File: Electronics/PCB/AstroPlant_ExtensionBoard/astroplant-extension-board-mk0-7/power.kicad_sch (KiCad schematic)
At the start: 13 parts, among them J14 61300621121, J20 691102710002, J21 691102710002

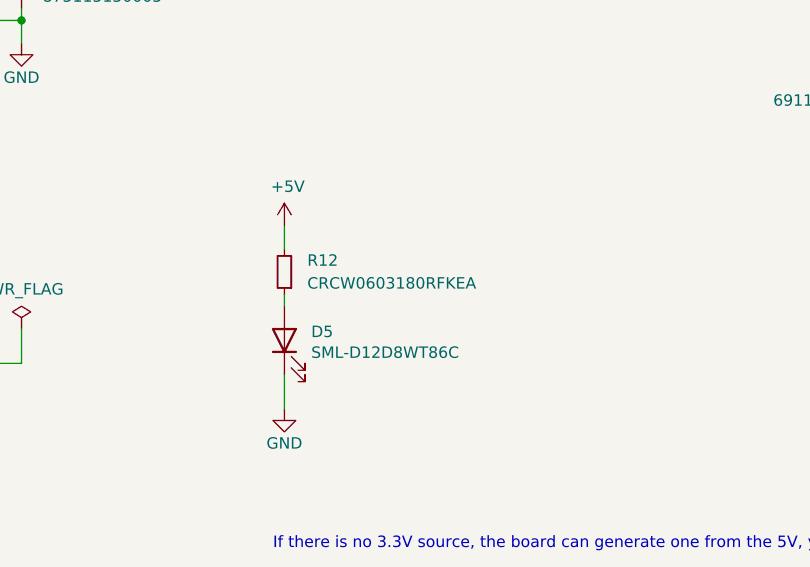
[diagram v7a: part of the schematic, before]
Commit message: Fix the antenna (Implies a change in PCB routing)+ improve readme (add a tutorial to make the board on eurocicruit).
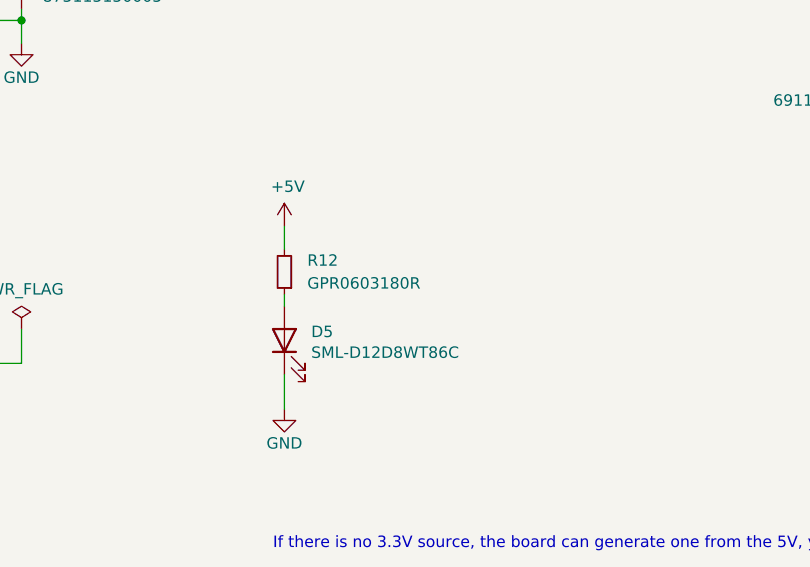
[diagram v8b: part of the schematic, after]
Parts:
- C15: footprint CAPC1608X50N -> Capacitor_SMD:C_0603_1608Metric; Arrow Price/Stock https://www.arrow.com/en/products/grm185r61c105ke44d/murata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 -> (none); Height 0.5 -> (none); MPN GRM185R61C105KE44D -> GPC0603105-16; Manufacturer_Name Murata Electronics -> (none); Manufacturer_Part_Number GRM185R61C105KE44D -> (none); Mouser Part Number 81-GRM185R61C105KE44 -> (none); Mouser Price/Stock https://www.mouser.co.uk/ProductDetail/Murata-Electronics/G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 -> (none)
- C16: footprint CAPC1608X50N -> Capacitor_SMD:C_0603_1608Metric; Arrow Price/Stock https://www.arrow.com/en/products/grm185r61c105ke44d/murata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 -> (none); Height 0.5 -> (none); MPN GRM185R61C105KE44D -> GPC0603105-16; Manufacturer_Name Murata Electronics -> (none); Manufacturer_Part_Number GRM185R61C105KE44D -> GPC0603105-16; Mouser Part Number 81-GRM185R61C105KE44 -> (none); Mouser Price/Stock https://www.mouser.co.uk/ProductDetail/Murata-Electronics/G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 -> (none)
- R12: value CRCW0603180RFKEA -> GPR0603180R; MPN CRCW0603180RFKEA -> GPR0603180R
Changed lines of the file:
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@@
       (effects (font (size 1.27 1.27)) (justify left))
     )
-    (property "Footprint" "CAPC1608X50N" (at 231.14 153.67 0)
-      (effects (font (size 1.27 1.27)) (justify left) hide)
-    )
-    (property "Datasheet" "https://componentsearchengine.com/Datasheets/2/GRM185R61C105KE44D.pdf" (at 228.6 153.67 0)
-      (effects (font (size 1.27 1.27)) (justify left) hide)
-    )
-    (property "Description" "MURATA - GRM185R61C105KE44D - CAP, MLCC, X5R, 1UF, 16V, 0603" (at 226.06 153.67 0)
-      (effects (font (size 1.27 1.27)) (justify left) hide)
-    )
-    (property "Height" "0.5" (at 223.52 153.67 0)
-      (effects (font (size 1.27 1.27)) (justify left) hide)
-    )
-    (property "Manufacturer_Name" "Murata Electronics" (at 220.98 153.67 0)
-      (effects (font (size 1.27 1.27)) (justify left) hide)
-    )
-    (property "Manufacturer_Part_Number" "GRM185R61C105KE44D" (at 218.44 153.67 0)
-      (effects (font (size 1.27 1.27)) (justify left) hide)
-    )
-    (property "Mouser Part Number" "81-GRM185R61C105KE44" (at 215.9 153.67 0)
-      (effects (font (size 1.27 1.27)) (justify left) hide)
-    )
-    (property "Mouser Price/Stock" "https://www.mouser.co.uk/ProductDetail/Murata-Electronics/GRM185R61C105KE44D?qs=c4yvaafl%252BAw5enNBKMnY3A%3D%3D" (at 213.36 153.67 0)
-      (effects (font (size 1.27 1.27)) (justify left) hide)
-    )
-    (property "MPN" "GRM185R61C105KE44D" (at 210.82 153.67 0)
-      (effects (font (size 1.27 1.27)) (justify left) hide)
-    )
-    (property "Arrow Price/Stock" "https://www.arrow.com/en/products/grm185r61c105ke44d/murata-manufacturing" (at 208.28 153.67 0)
+    (property "Footprint" "Capacitor_SMD:C_0603_1608Metric" (at 231.14 153.67 0)
+      (effects (font (size 1.27 1.27)) (justify left) hide)
+    )
+    (property "Datasheet" "" (at 228.6 153.67 0)
+      (effects (font (size 1.27 1.27)) (justify left) hide)
+    )
+    (property "Manufacturer_Part_Number" "GPC0603105-16" (at 218.44 153.67 0)
+      (effects (font (size 1.27 1.27)) (justify left) hide)
+    )
+    (property "MPN" "GPC0603105-16" (at 210.82 153.67 0)
       (effects (font (size 1.27 1.27)) (justify left) hide)
     )
@@
       (effects (font (size 1.27 1.27)) (justify right))
     )
-    (property "Value" "CRCW0603180RFKEA" (at 120.65 99.06 0)
+    (property "Value" "GPR0603180R" (at 120.65 99.06 0)
       (effects (font (size 1.27 1.27)) (justify right))
     )
@@
       (effects (font (size 1.27 1.27)) hide)
     )
-    (property "MPN" "CRCW0603180RFKEA" (at 118.11 97.79 0)
+    (property "MPN" "GPR0603180R" (at 118.11 97.79 0)
       (effects (font (size 1.27 1.27)) hide)
     )
@@
       (effects (font (size 1.27 1.27)) (justify left))
     )
-    (property "Footprint" "CAPC1608X50N" (at 181.61 148.59 0)
-      (effects (font (size 1.27 1.27)) (justify left) hide)
-    )
-    (property "Datasheet" "https://componentsearchengine.com/Datasheets/2/GRM185R61C105KE44D.pdf" (at 179.07 148.59 0)
-      (effects (font (size 1.27 1.27)) (justify left) hide)
-    )
-    (property "Description" "MURATA - GRM185R61C105KE44D - CAP, MLCC, X5R, 1UF, 16V, 0603" (at 176.53 148.59 0)
-      (effects (font (size 1.27 1.27)) (justify left) hide)
-    )
-    (property "Height" "0.5" (at 173.99 148.59 0)
-      (effects (font (size 1.27 1.27)) (justify left) hide)
-    )
-    (property "Manufacturer_Name" "Murata Electronics" (at 171.45 148.59 0)
-      (effects (font (size 1.27 1.27)) (justify left) hide)
-    )
-    (property "Manufacturer_Part_Number" "GRM185R61C105KE44D" (at 168.91 148.59 0)
-      (effects (font (size 1.27 1.27)) (justify left) hide)
-    )
-    (property "Mouser Part Number" "81-GRM185R61C105KE44" (at 166.37 148.59 0)
-      (effects (font (size 1.27 1.27)) (justify left) hide)
-    )
-    (property "Mouser Price/Stock" "https://www.mouser.co.uk/ProductDetail/Murata-Electronics/GRM185R61C105KE44D?qs=c4yvaafl%252BAw5enNBKMnY3A%3D%3D" (at 163.83 148.59 0)
-      (effects (font (size 1.27 1.27)) (justify left) hide)
-    )
-    (property "MPN" "GRM185R61C105KE44D" (at 161.29 148.59 0)
-      (effects (font (size 1.27 1.27)) (justify left) hide)
-    )
-    (property "Arrow Price/Stock" "https://www.arrow.com/en/products/grm185r61c105ke44d/murata-manufacturing" (at 158.75 148.59 0)
-      (effects (font (size 1.27 1.27)) (justify left) hide)
-    )
+    (property "Footprint" "Capacitor_SMD:C_0603_1608Metric" (at 181.61 148.59 0)
+      (effects (font (size 1.27 1.27)) (justify left) hide)
+    )
+    (property "Datasheet" "" (at 179.07 148.59 0)
+      (effects (font (size 1.27 1.27)) (justify left) hide)
+    )
+    (property "MPN" "GPC0603105-16" (at 161.29 148.59 0)
+      (effects (font (size 1.27 1.27)) (justify left) hide)
+    )
